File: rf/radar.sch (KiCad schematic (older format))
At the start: 12 parts, among them J101 Conn_01x03, J102 Conn_Coaxial, J103 Conn_01x04, J104 Conn_01x03, J105 Conn_01x03, J106 Conn_Coaxial, J107 Conn_01x02, U101 CP0402Q5425ENTR

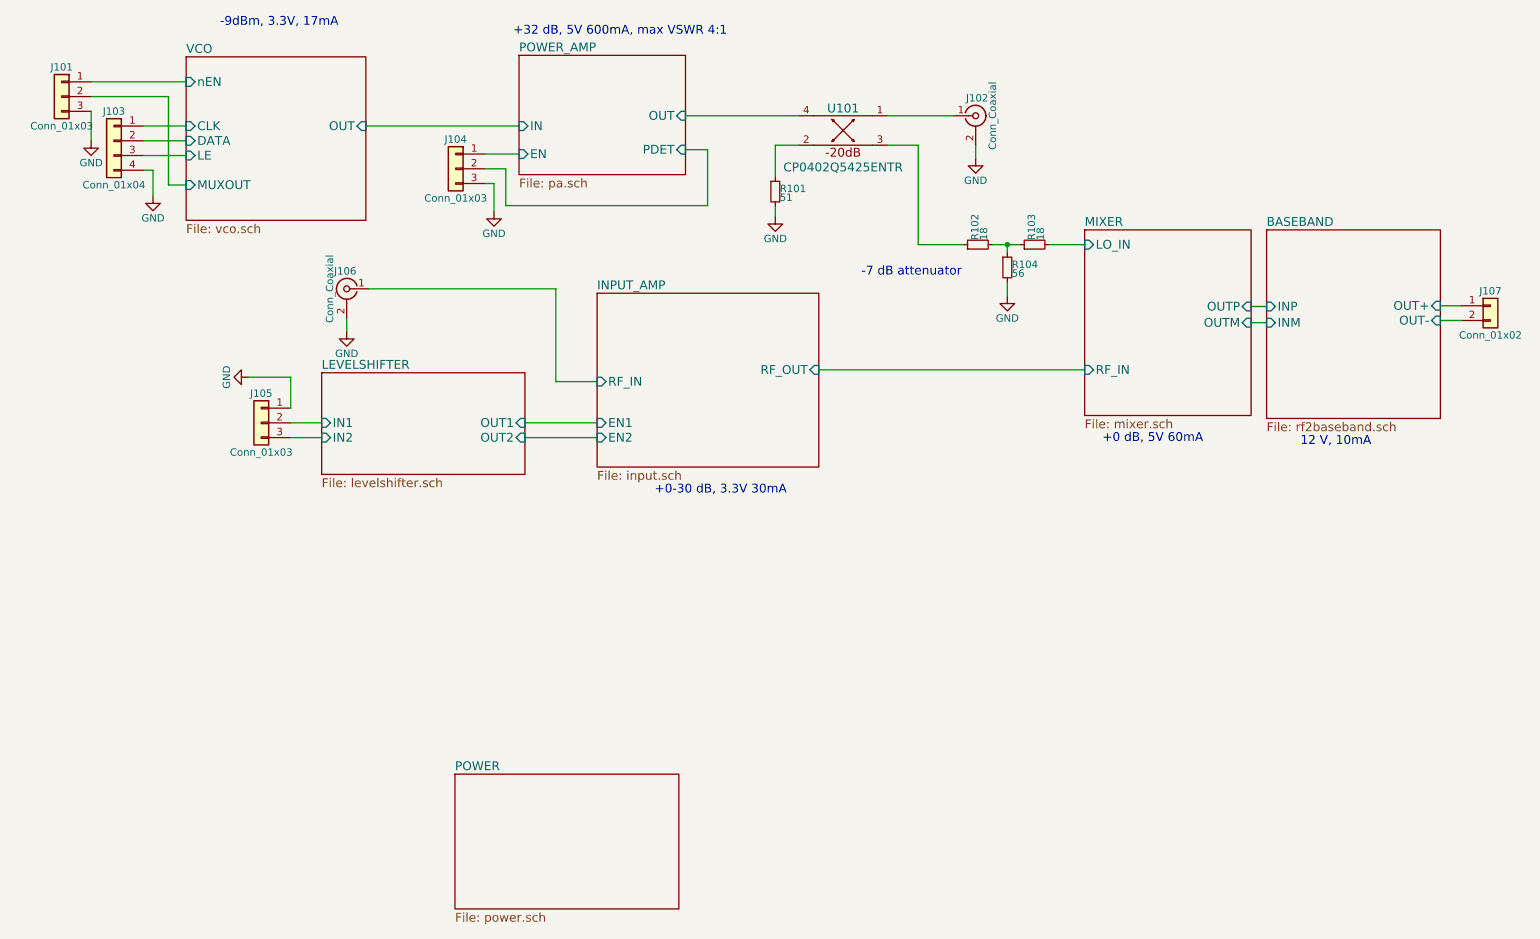
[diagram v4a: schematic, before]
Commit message: Line up connectors across both boards, spread out component footprints
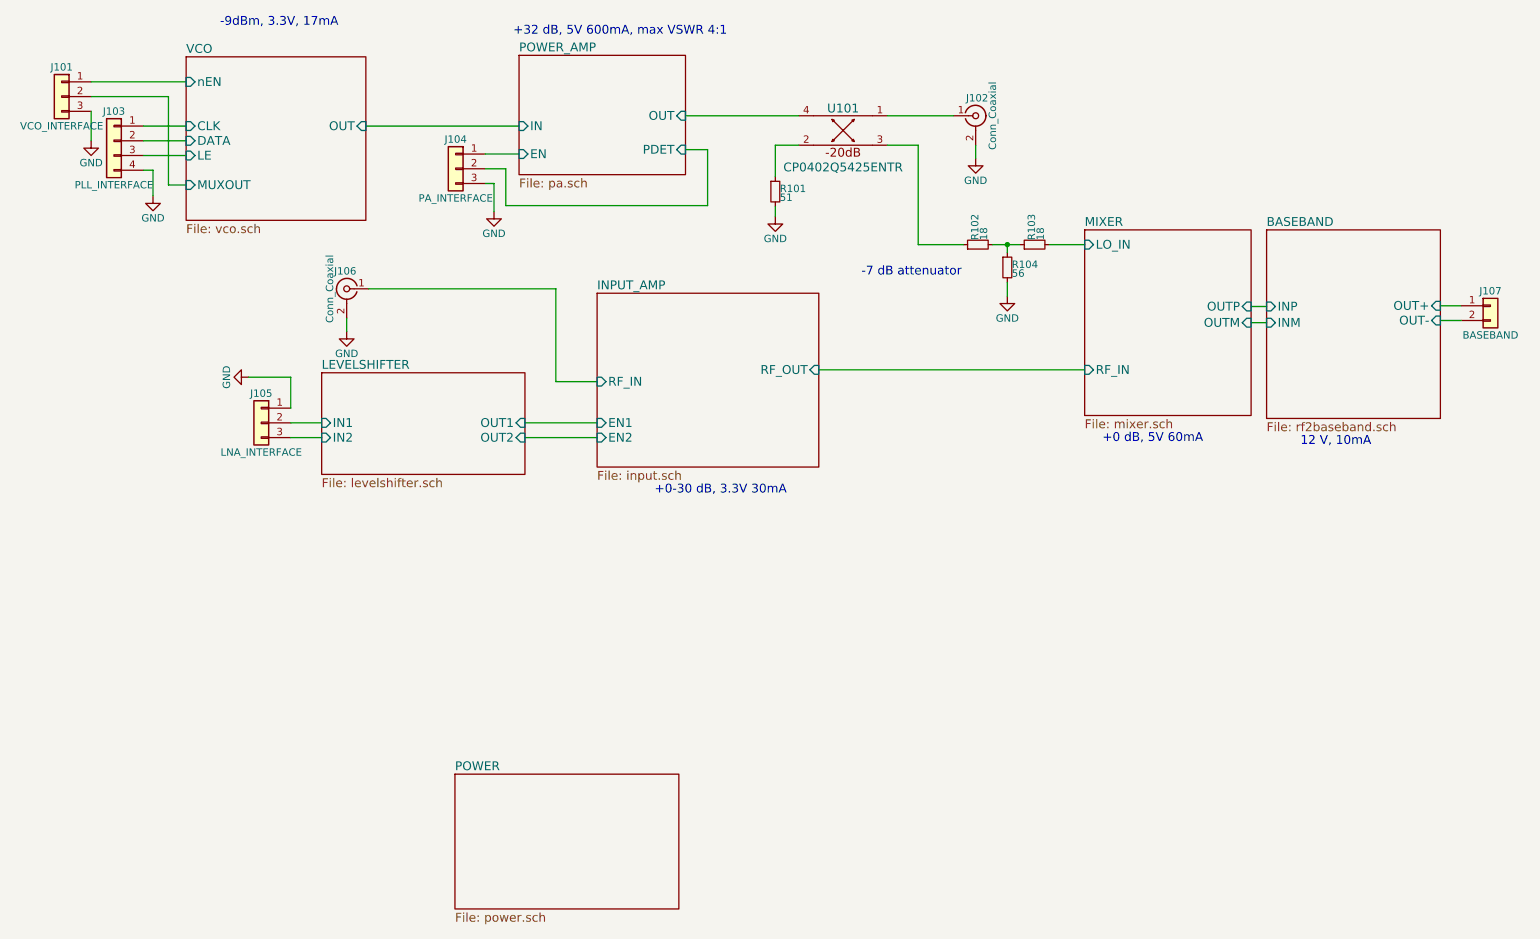
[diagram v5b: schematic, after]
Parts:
- J101: value Conn_01x03 -> VCO_INTERFACE
- J103: value Conn_01x04 -> PLL_INTERFACE
- J104: value Conn_01x03 -> PA_INTERFACE
- J105: value Conn_01x03 -> LNA_INTERFACE
- J107: value Conn_01x02 -> BASEBAND
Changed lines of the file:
@@
 P 10550 2870
 F 0 "J107" H 10550 2970 50  0000 C CNN
-F 1 "Conn_01x02" H 10550 2670 50  0000 C CNN
+F 1 "BASEBAND" H 10550 2670 50  0000 C CNN
 F 2 "Pin_Headers:Pin_Header_Straight_1x02_Pitch2.54mm" H 10550 2870 50  0001 C CNN
 F 3 "" H 10550 2870 50  0001 C CNN
@@
 P 1205 1750
 F 0 "J103" H 1205 1950 50  0000 C CNN
-F 1 "Conn_01x04" H 1205 1450 50  0000 C CNN
+F 1 "PLL_INTERFACE" H 1205 1450 50  0000 C CNN
 F 2 "Socket_Strips:Socket_Strip_Straight_1x04_Pitch2.54mm" H 1205 1750 50  0001 C CNN
 F 3 "" H 1205 1750 50  0001 C CNN
@@
 P 3525 1940
 F 0 "J104" H 3525 2140 50  0000 C CNN
-F 1 "Conn_01x03" H 3525 1740 50  0000 C CNN
+F 1 "PA_INTERFACE" H 3525 1740 50  0000 C CNN
 F 2 "Socket_Strips:Socket_Strip_Straight_1x03_Pitch2.54mm" H 3525 1940 50  0001 C CNN
 F 3 "" H 3525 1940 50  0001 C CNN
@@
 P 2205 3665
 F 0 "J105" H 2205 3865 50  0000 C CNN
-F 1 "Conn_01x03" H 2205 3465 50  0000 C CNN
+F 1 "LNA_INTERFACE" H 2205 3465 50  0000 C CNN
 F 2 "Socket_Strips:Socket_Strip_Straight_1x03_Pitch2.54mm" H 2205 3665 50  0001 C CNN
 F 3 "" H 2205 3665 50  0001 C CNN
@@
 P 850 1450
 F 0 "J101" H 850 1650 50  0000 C CNN
-F 1 "Conn_01x03" H 850 1250 50  0000 C CNN
+F 1 "VCO_INTERFACE" H 850 1250 50  0000 C CNN
 F 2 "Socket_Strips:Socket_Strip_Straight_1x03_Pitch2.54mm" H 850 1450 50  0001 C CNN
 F 3 "" H 850 1450 50  0001 C CNN
